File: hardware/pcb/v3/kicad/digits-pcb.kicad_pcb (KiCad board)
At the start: 2 copper layers, 61.9 x 76.2 mm, 77 parts, among them J8 Conn_01x04, SW1 Hook_DPDT, SW2 SW_Push, U10 XL6019E1, U2 DRV8871DDAR, U3 RP2040, U4 W25Q16JVSSIQ, U5 AMS1117-3.3, U6 TLV320AIC3104IRHBR, U7 XC6206P182MR, Y1 ABM8-272-T3

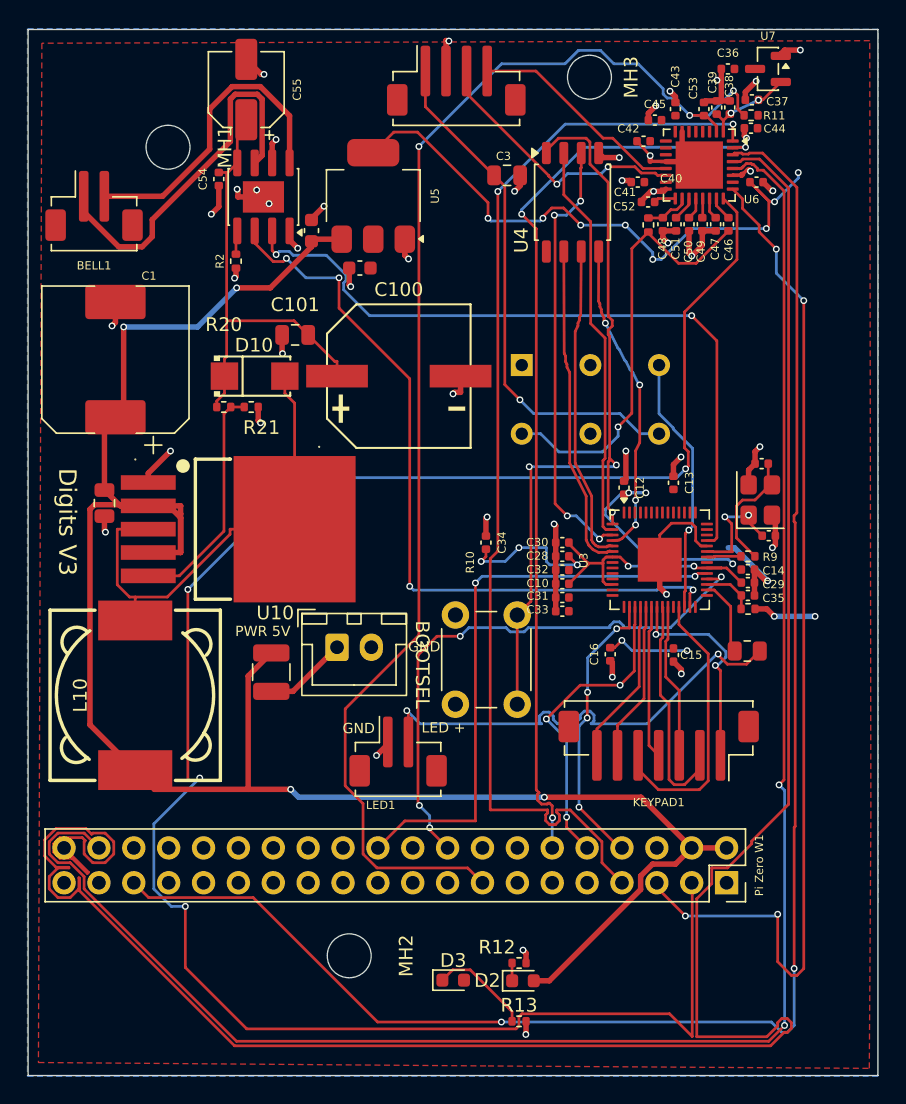
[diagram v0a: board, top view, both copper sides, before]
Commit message: fix(hardware): restore EP ground vias and repair the Switching netclass pattern
Heavy rerouting this session had left the codec (U6), bell driver (U2),
and RP2040 (U3) exposed-pad ground stitching short of the known-good V2
counts (0/2/0 vs V2's 4/4/1). Restored them to 4/4/1, all on GND, placed
clear of the +3V3/DVDD traces that run on B.Cu under the RP2040 pad.
Leftover dangling vias from the reroute were also cleaned.

The "Switching" netclass pattern targeted bare net name SW_NODE, but the
boost switch node is /ringer/SW_NODE (hierarchical prefix), so its 0.75mm
width rule was silently void. Corrected the pattern. Existing SW_NODE
tracks stay 0.2mm pending a boost-area re-route decision (the net is too
boxed-in by the +3V3 zone, U10 pad, and FB divider to widen in place).
DRC clean: 0 errors, 0 unconnected, 0 parity.
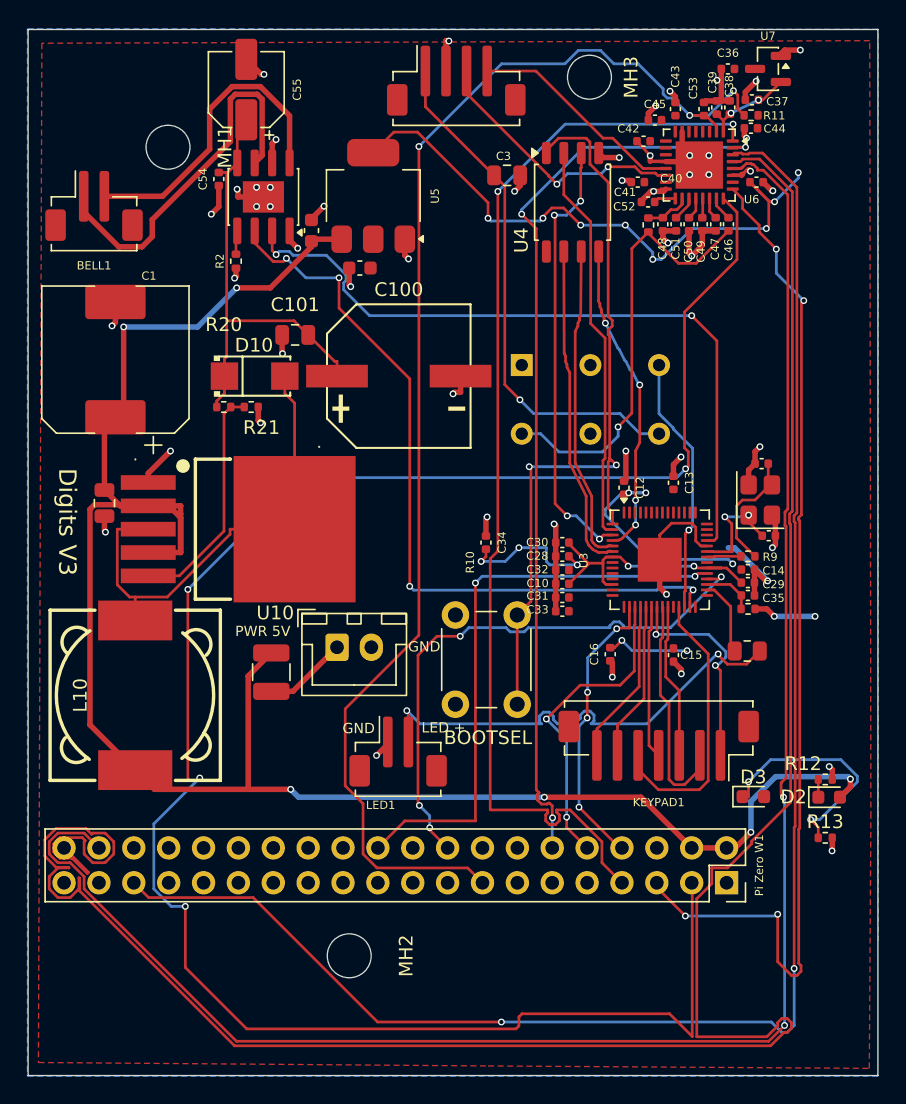
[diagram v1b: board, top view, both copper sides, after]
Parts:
- moved R12 26.0 mm to (70.8, 66.8)
- moved R13 26.0 mm to (70.8, 71.1)
- moved D2 26.0 mm to (71.1, 68.1)
- moved D3 25.6 mm to (65.6, 68.1)
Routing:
- net /LED3V3_K: track 7.35 -> 16.7 mm, vias 0 -> 2
- net +5V: track 145.2 -> 143.3 mm, vias 4 -> 6
- net GND: vias 46 -> 52
- net UART_RX_PI: vias 3 -> 2
- net QSPI_SS: vias 3 -> 2

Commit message: fix(hardware): widen boost SW_NODE to 0.75mm and clean reroute stubs
Re-routed the boost corner to make room and widened /ringer/SW_NODE from
0.2mm to the netclass-intended 0.75mm, still front-only with no vias per
the switching-node rules, so the boost inductor current has adequate
trace capacity. Ran Cleanup Tracks and Vias to drop leftover dangling
stubs and merge co-linear segments. DRC clean: 0 errors, 0 unconnected,
0 parity, 0 dangling.
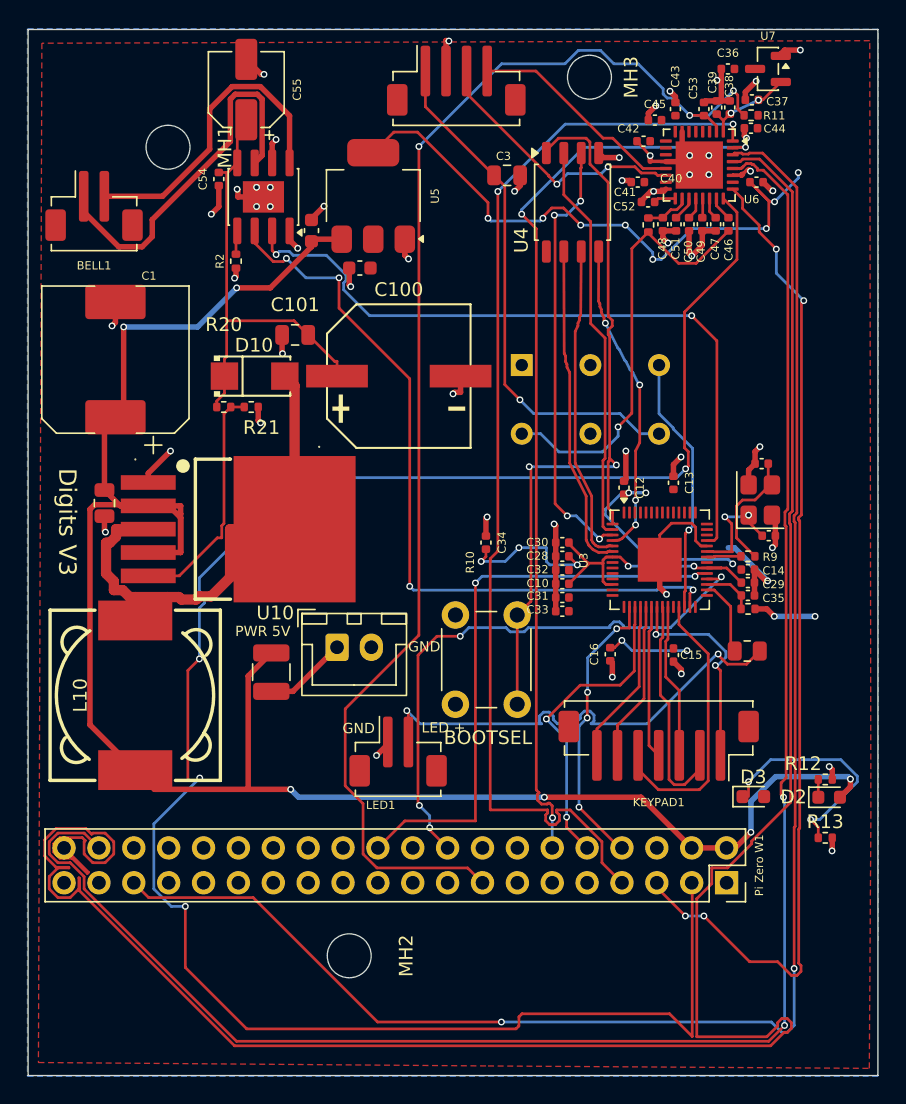
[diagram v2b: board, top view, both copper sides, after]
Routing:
- net /ringer/SW_NODE: track 35.0 -> 38.3 mm
- net CODEC_SCL: track 75.2 -> 73.0 mm

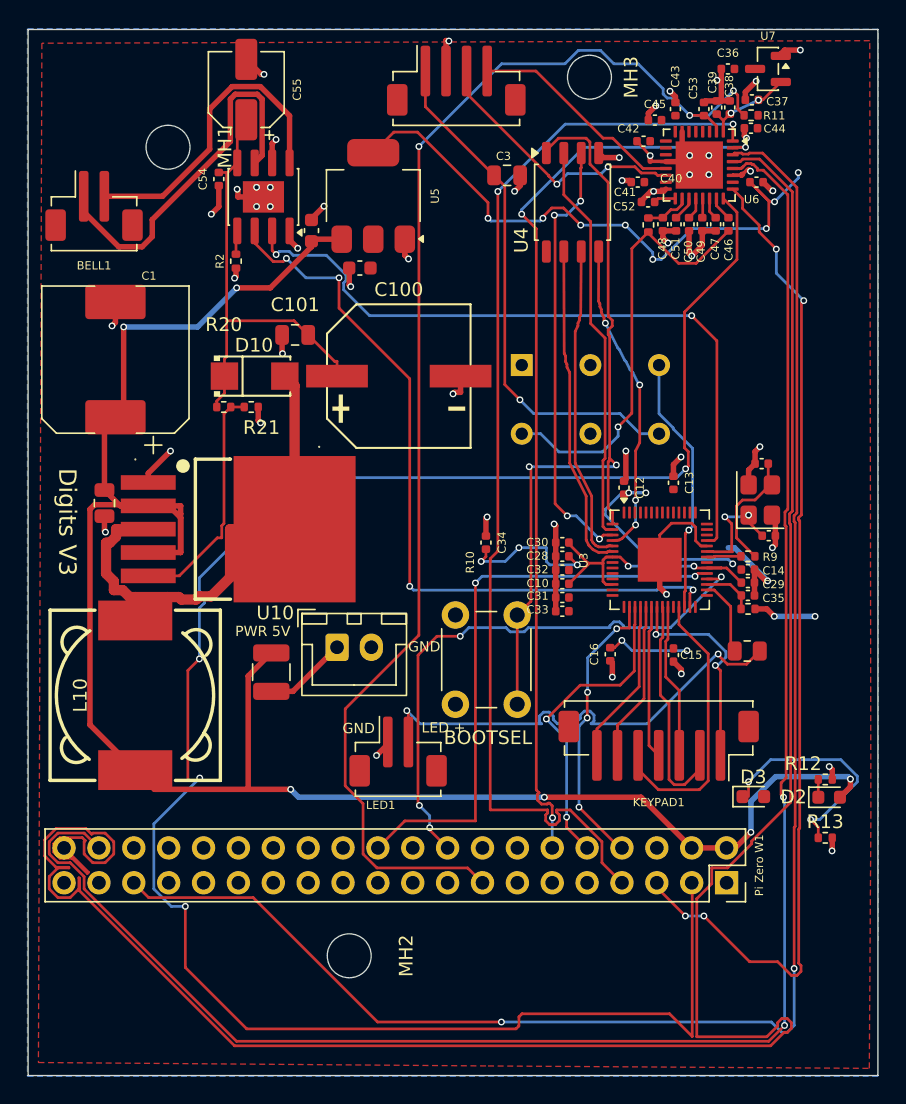
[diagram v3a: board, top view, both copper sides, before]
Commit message: fix(hardware): finalize V3 PCB for first fab (#632)
Rename the Pi header reference to PI_ZERO_W1 (the old "Pi Zero W1" had
spaces, which JLCPCB splits, breaking BOM/CPL designator matching so the
header silently dropped from assembly), correct R13 to the real 120R
part C25079, and bring the boost SW_NODE width and min-width rule, EP
ground vias, Pi-header mating mirror, and SW1 DPDT pin map into main.
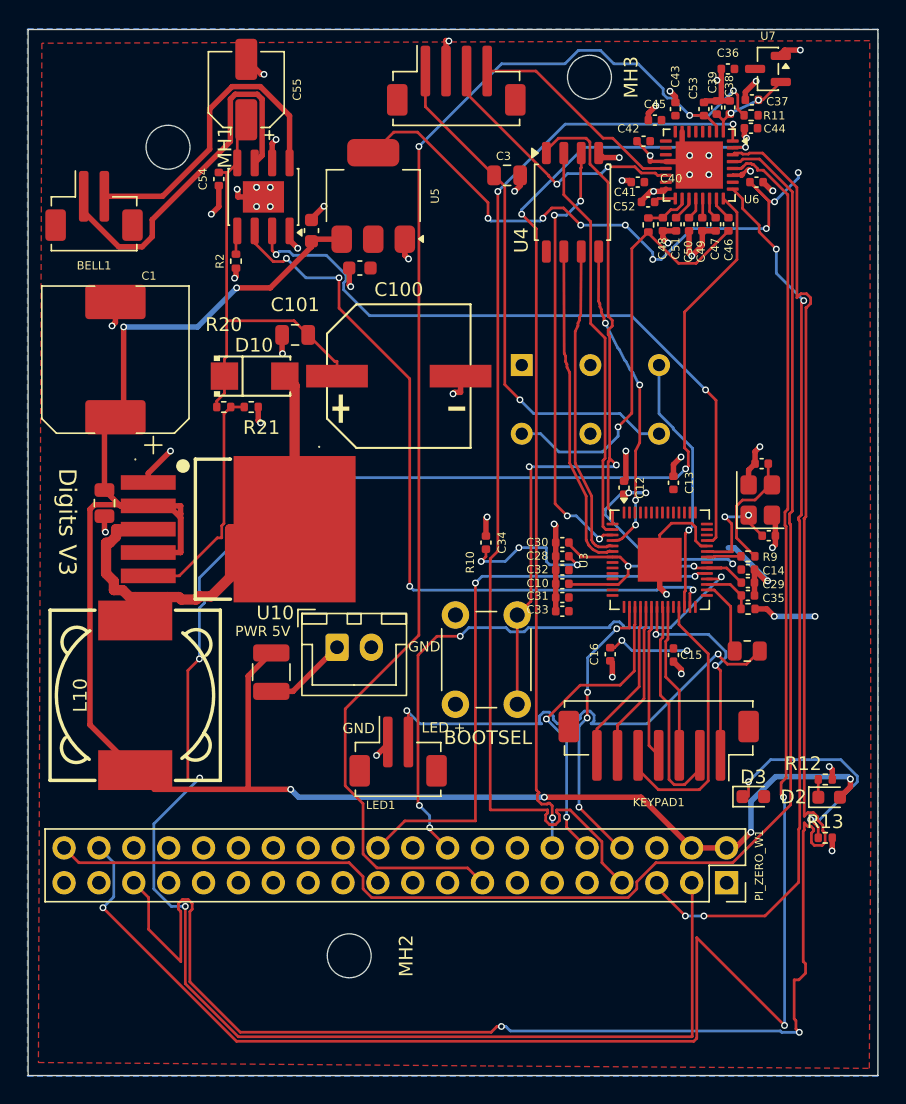
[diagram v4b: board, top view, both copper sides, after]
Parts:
- PI_ZERO_W1: renamed from Pi Zero W1
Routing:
- net CODEC_DIN: track 165.5 -> 108.2 mm
- net CODEC_WCLK: track 119.9 -> 140.3 mm
- net CODEC_SCL: track 73.0 -> 65.4 mm
- net CODEC_DOUT: track 131.5 -> 135.1 mm, vias 2 -> 3
- net RINGER_IN2: track 52.8 -> 50.1 mm
- net CODEC_SDA: track 145.2 -> 144.6 mm
- net DVDD_1V1: track 19.6 -> 20.2 mm

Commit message: fix(hardware): correct V3 PCB Y-mirrored footprints, restore nets, add thermal vias
All IC footprints in V3 had Y-mirrored pad coordinates from an early
front/back flip during board creation. Every IC would have had pins
connected to wrong nets. Updated all footprints from the KiCad library
to restore correct pad geometry.

Additional fixes:
- Restored net assignments on PI_ZERO_W1 (40-pin Pi header) and U6
  (TLV320AIC3104 codec) that were lost during footprint repair
- Added GND thermal vias under U3 (RP2040, 3x3), U6 (TLV320AIC3104,
  3x3), and U2 (DRV8871, 2x2) exposed pads
- Fixed layer stackup metadata: F.SilkS/B.SilkS/F.CrtYd/B.CrtYd user
  names were swapped from the original flip operation
- Removed dangling MIC_FROM_SW via and XOUT_MCU track stubs
- Added no-connect flag on SW1 pin 5 (unused pole B throw)
- Fixed R13 LCSC part number in COMPONENTS.md (C25752 to C25079)
- Updated NET_TOPOLOGY.md mounting hole coordinates to actual V3
  positions (were stale V2 values since initial creation)
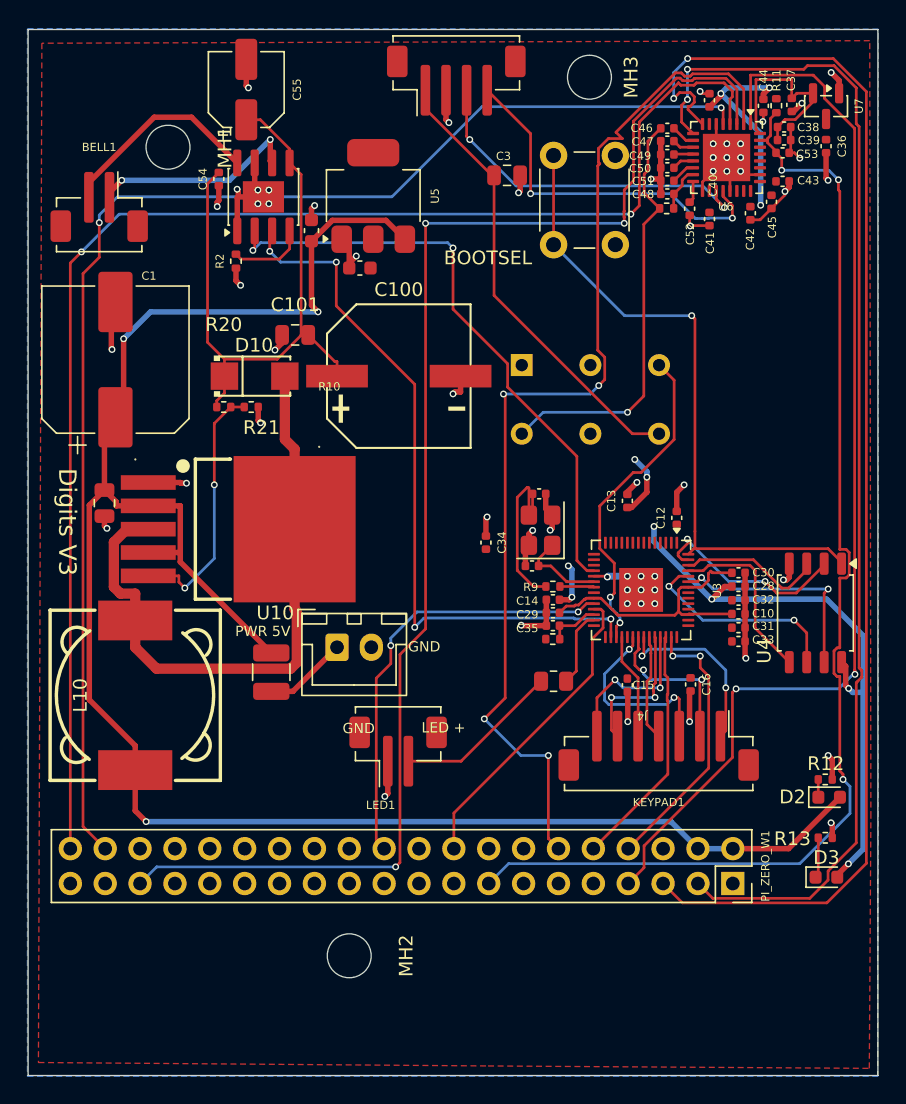
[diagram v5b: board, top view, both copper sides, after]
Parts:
- moved U4 34.8 mm to (70.1, 54.7)
- moved SW2 33.6 mm to (51.0, 27.9)
- moved C5 17.4 mm to (49.5, 51.3), turned to 180 degrees
- moved C6 16.4 mm to (50.0, 46.0), turned to 0 degrees
- moved Y1 16.2 mm to (50.1, 48.7)
- moved R5 14.4 mm to (51.0, 56.6), turned to 0 degrees
- moved R9 14.4 mm to (51.0, 52.8), turned to 180 degrees
- moved C35 14.4 mm to (51.0, 55.6), turned to 180 degrees
- moved C14 14.4 mm to (51.0, 53.7), turned to 180 degrees
- moved C29 14.4 mm to (51.0, 54.7), turned to 180 degrees
- moved R1 14.3 mm to (51.0, 59.7), turned to 180 degrees
- moved C10 13.0 mm to (64.5, 54.8), turned to 0 degrees
- moved C28 13.0 mm to (64.5, 52.8), turned to 0 degrees
- moved C30 13.0 mm to (64.5, 51.8), turned to 0 degrees
- moved C31 13.0 mm to (64.5, 55.8), turned to 0 degrees
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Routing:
- net CODEC_SDA: track 144.6 -> 87.6 mm, vias 4 -> 2
- net CODEC_WCLK: track 140.3 -> 101.0 mm, vias 2 -> 3
- net CODEC_DOUT: track 135.1 -> 97.2 mm, vias 3 -> 2
- net CODEC_SCL: track 65.4 -> 94.7 mm, vias 4 -> 2
- net LED_A: track 34.2 -> 12.1 mm, vias 2 -> 0
- net QSPI_SD2: track 32.3 -> 10.7 mm, vias 4 -> 0
- net SWD_SWDIO: track 41.3 -> 22.5 mm, vias 4 -> 0
- net +3V3: track 82.5 -> 66.1 mm, vias 18 -> 11
- net QSPI_SD1: track 29.3 -> 15.0 mm, vias 0 -> 2
- net /ringer/VBOOST: track 32.8 -> 46.9 mm
- net /LED3V3_K: track 16.7 -> 2.95 mm, vias 2 -> 0
- net KP_ROW2: track 20.6 -> 7.70 mm
- net CODEC_BCLK: track 67.1 -> 79.1 mm, vias 3 -> 4
- net BELL_A: track 27.3 -> 15.4 mm, vias 0 -> 2
- net CODEC_RESET: track 97.4 -> 86.5 mm
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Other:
- board text added: "J4"
